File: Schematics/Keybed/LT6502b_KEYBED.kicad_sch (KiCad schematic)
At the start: 30 parts, among them J14 KeyConn, J4 Conn_02x05_Odd_Even, Q3 STL9P3LLH6, U2 74HCT138, U3 ATmega644P-20A, X2 CXO_DIP8

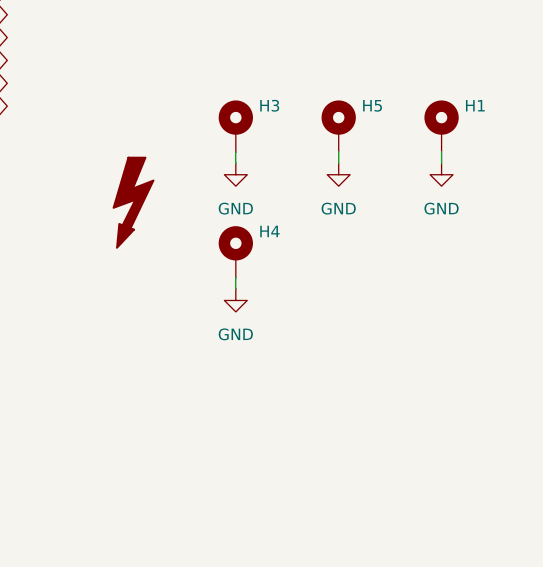
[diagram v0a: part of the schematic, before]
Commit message: Add extra mounting holes
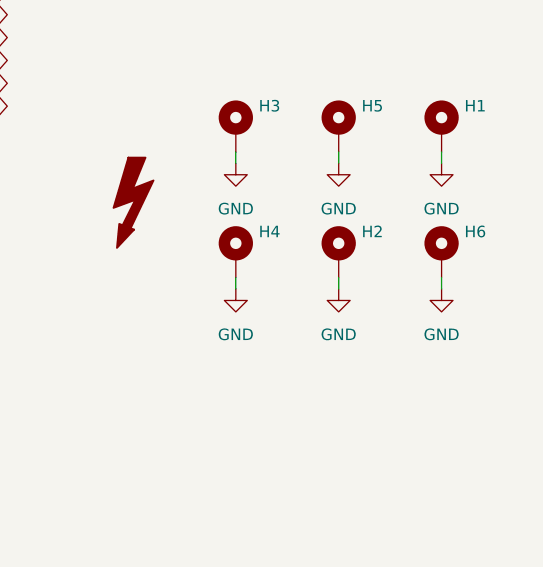
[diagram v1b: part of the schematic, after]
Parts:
- added H2, H6: MountingHole_Pad, MountingHole:MountingHole_3.2mm_M3_Pad_TopBottom, symbol Mechanical:MountingHole_Pad
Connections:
- net GND: now also H2.1, H6.1
